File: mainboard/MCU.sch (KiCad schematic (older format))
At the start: 49 parts, among them J12 SPARE_PINS, J9 Micro_SD_Card_Det_Hirose_DM3AT, SW1 RESET, U12 M95256-WMN6P, U5 MCP2562, U6 LM358, U9 STM32F446RE_64PIN, Y1 26MHz

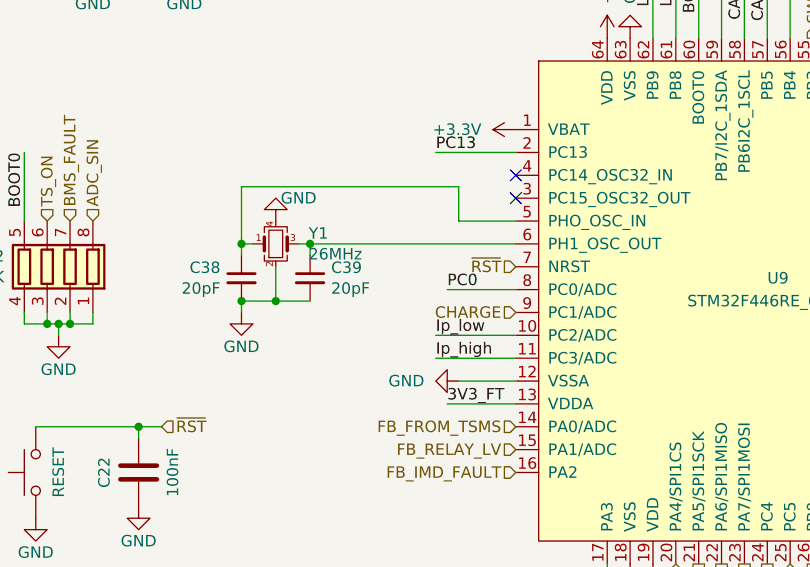
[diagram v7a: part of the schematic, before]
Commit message: Renamed handcart detection
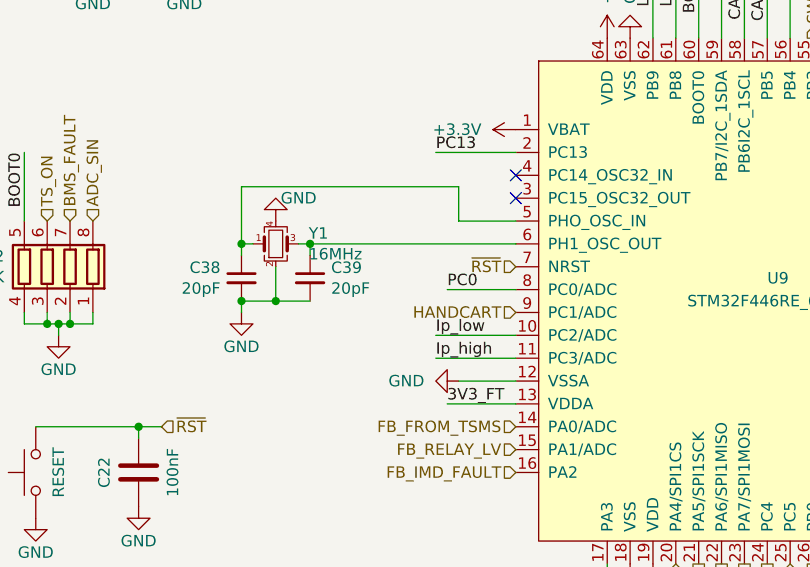
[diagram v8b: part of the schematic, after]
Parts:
- Y1: value 26MHz -> 16MHz
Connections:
- net CHARGE renamed HANDCART
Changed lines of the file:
@@
 $EndComp
 Text HLabel 7850 2550 0    50   Input ~ 0
-CHARGE
+HANDCART
 Text Label 8850 1000 3    50   ~ 0
 CAN_TX
@@
 P 6800 2250
 F 0 "Y1" H 6944 2296 50  0000 L CNN
-F 1 "26MHz" H 6944 2205 50  0000 L CNN
+F 1 "16MHz" H 6944 2205 50  0000 L CNN
 F 2 "Crystal:Crystal_SMD_3225-4Pin_3.2x2.5mm" H 6800 2250 50  0001 C CNN
 F 3 "~" H 6800 2250 50  0001 C CNN
